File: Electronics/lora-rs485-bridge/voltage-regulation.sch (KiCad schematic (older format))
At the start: 5 parts, among them U4 MCP1810T-33I_OT

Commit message: Some PCB routing is done
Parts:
- C11: renamed from C?; footprint zive:C_0603_1608Metric -> Capacitor_SMD:C_0603_1608Metric
- C16, C7: footprint zive:C_0603_1608Metric -> Capacitor_SMD:C_0603_1608Metric
- R2: renamed from R?; footprint (none) -> Resistor_SMD:R_0603_1608Metric
- U4: footprint zive:SOT-23-5 -> Package_TO_SOT_SMD:SOT-23-5
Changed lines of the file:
@@
 EESchema Schematic File Version 5
-LIBS:lora-bridge-cache
 EELAYER 30 0
 EELAYER END
 $Descr A4 11693 8268
 encoding utf-8
-Sheet 4 5
+Sheet 3 5
 Title ""
 Date ""
@@
 F 0 "C7" H 3560 1771 50  0000 R CNN
 F 1 "4.7u" H 3560 1680 50  0000 R CNN
-F 2 "zive:C_0603_1608Metric" H 3713 1575 50  0001 C CNN
+F 2 "Capacitor_SMD:C_0603_1608Metric" H 3713 1575 50  0001 C CNN
 F 3 "~" H 3675 1725 50  0001 C CNN
 F 4 "CL10A475KP8NNNC" H 3675 1725 50  0001 C CNN "PartNo"
@@
 F 0 "U4" H 4600 2100 50  0000 C CNN
 F 1 "MCP1810T-33I_OT" H 4600 2009 50  0000 C CNN
-F 2 "zive:SOT-23-5" H 4625 1525 50  0001 C CNN
+F 2 "Package_TO_SOT_SMD:SOT-23-5" H 4625 1525 50  0001 C CNN
 F 3 "" H 4625 1525 50  0001 C CNN
 F 4 "MICROCHIP" H 4625 1725 50  0001 C CNN "Manufacturer"
@@
 F 0 "C16" H 3160 1771 50  0000 R CNN
 F 1 "4.7u" H 3160 1680 50  0000 R CNN
-F 2 "zive:C_0603_1608Metric" H 3313 1575 50  0001 C CNN
+F 2 "Capacitor_SMD:C_0603_1608Metric" H 3313 1575 50  0001 C CNN
 F 3 "~" H 3275 1725 50  0001 C CNN
 F 4 "CL10A475KP8NNNC" H 3275 1725 50  0001 C CNN "PartNo"
@@
 	5275 1575 5450 1575
 $Comp
-L Device:C C?
+L Device:C C11
 U 1 1 5D86D7BC
 P 5450 2025
-F 0 "C?" H 5335 2071 50  0000 R CNN
+F 0 "C11" H 5335 2071 50  0000 R CNN
 F 1 "4.7u" H 5335 1980 50  0000 R CNN
-F 2 "zive:C_0603_1608Metric" H 5488 1875 50  0001 C CNN
+F 2 "Capacitor_SMD:C_0603_1608Metric" H 5488 1875 50  0001 C CNN
 F 3 "~" H 5450 2025 50  0001 C CNN
 F 4 "CL10A475KP8NNNC" H 5450 2025 50  0001 C CNN "PartNo"
@@
 $EndComp
 $Comp
-L Device:R R?
+L Device:R R2
 U 1 1 5D86E8A3
 P 5450 1725
-F 0 "R?" H 5520 1771 50  0000 L CNN
+F 0 "R2" H 5520 1771 50  0000 L CNN
 F 1 "0" H 5520 1680 50  0000 L CNN
-F 2 "" V 5380 1725 50  0001 C CNN
+F 2 "Resistor_SMD:R_0603_1608Metric" V 5380 1725 50  0001 C CNN
 F 3 "~" H 5450 1725 50  0001 C CNN
 	1    5450 1725

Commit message: Add ESD protection to i2c lines, change VIN TVS diode to higher voltage, add series resistors to SPI lines, compress the PCB to be at width of typical 4xAA battery holder
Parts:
- removed R2: 0, Resistor_SMD:R_0603_1608Metric, symbol Device:R
- removed U4: MCP1810T-33I_OT, Package_TO_SOT_SMD:SOT-23-5, symbol miceuz:MCP1810T-33I_OT
- added U4: NCP718, TO_SOT_Packages_SMD:SOT-23-5, symbol miceuz:NCP718
- C11, C16, C7: Manufacturer SAMSUNG -> TDK; PartNo CL10A475KP8NNNC -> C1608X5R1C475K080AE
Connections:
- wire segments 9 -> 10
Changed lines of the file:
@@
 $Descr A4 11693 8268
 encoding utf-8
-Sheet 3 5
+Sheet 2 5
 Title ""
 Date ""
@@
 Text HLabel 4625 2175 3    50   Input ~ 0
 GND
-Text HLabel 5450 1575 2    50   Input ~ 0
-VOUT
 $Comp
 L Device:C C7
@@
 F 2 "Capacitor_SMD:C_0603_1608Metric" H 3713 1575 50  0001 C CNN
 F 3 "~" H 3675 1725 50  0001 C CNN
-F 4 "CL10A475KP8NNNC" H 3675 1725 50  0001 C CNN "PartNo"
-F 5 "SAMSUNG" H 3675 1725 50  0001 C CNN "Manufacturer"
+F 4 "C1608X5R1C475K080AE" H 3675 1725 50  0001 C CNN "PartNo"
+F 5 "TDK" H 3675 1725 50  0001 C CNN "Manufacturer"
 	1    3675 1725
 	1    0    0    -1
 $EndComp
-$Comp
-L miceuz:MCP1810T-33I_OT U4
-U 1 1 5C710FF3
-P 4625 1725
-F 0 "U4" H 4600 2100 50  0000 C CNN
-F 1 "MCP1810T-33I_OT" H 4600 2009 50  0000 C CNN
-F 2 "Package_TO_SOT_SMD:SOT-23-5" H 4625 1525 50  0001 C CNN
-F 3 "" H 4625 1525 50  0001 C CNN
-F 4 "MICROCHIP" H 4625 1725 50  0001 C CNN "Manufacturer"
-F 5 "MCP1810T-33I/OT" H 4625 1725 50  0001 C CNN "PartNo"
-	1    4625 1725
-	1    0    0    -1
-$EndComp
-Wire Wire Line
-	3925 1875 3925 1575
-Connection ~ 3925 1575
 Wire Wire Line
 	3675 1575 3925 1575
 Wire Wire Line
 	3675 1875 3675 2175
-Wire Wire Line
-	3675 2175 4625 2175
 $Comp
 L Device:C C16
@@
 F 2 "Capacitor_SMD:C_0603_1608Metric" H 3313 1575 50  0001 C CNN
 F 3 "~" H 3275 1725 50  0001 C CNN
-F 4 "CL10A475KP8NNNC" H 3275 1725 50  0001 C CNN "PartNo"
-F 5 "SAMSUNG" H 3275 1725 50  0001 C CNN "Manufacturer"
+F 4 "C1608X5R1C475K080AE" H 3275 1725 50  0001 C CNN "PartNo"
+F 5 "TDK" H 3275 1725 50  0001 C CNN "Manufacturer"
 	1    3275 1725
 	1    0    0    -1
@@
 	3275 1875 3275 2175
 Wire Wire Line
-	5450 2175 4625 2175
-Connection ~ 4625 2175
-Wire Wire Line
 	5275 1575 5450 1575
 $Comp
@@
 F 2 "Capacitor_SMD:C_0603_1608Metric" H 5488 1875 50  0001 C CNN
 F 3 "~" H 5450 2025 50  0001 C CNN
-F 4 "CL10A475KP8NNNC" H 5450 2025 50  0001 C CNN "PartNo"
-F 5 "SAMSUNG" H 5450 2025 50  0001 C CNN "Manufacturer"
+F 4 "C1608X5R1C475K080AE" H 5450 2025 50  0001 C CNN "PartNo"
+F 5 "TDK" H 5450 2025 50  0001 C CNN "Manufacturer"
 	1    5450 2025
 	1    0    0    -1
 $EndComp
+Wire Wire Line
+	3675 2175 4625 2175
 $Comp
-L Device:R R2
-U 1 1 5D86E8A3
-P 5450 1725
-F 0 "R2" H 5520 1771 50  0000 L CNN
-F 1 "0" H 5520 1680 50  0000 L CNN
-F 2 "Resistor_SMD:R_0603_1608Metric" V 5380 1725 50  0001 C CNN
-F 3 "~" H 5450 1725 50  0001 C CNN
-	1    5450 1725
+L miceuz:NCP718 U4
+U 1 1 5D8F1C6A
+P 4625 1725
+F 0 "U4" H 4600 2100 50  0000 C CNN
+F 1 "NCP718" H 4600 2009 50  0000 C CNN
+F 2 "TO_SOT_Packages_SMD:SOT-23-5" H 4625 1525 50  0001 C CNN
+F 3 "" H 4625 1525 50  0001 C CNN
+F 4 "NCP718ASN330T1G" H 4625 1725 50  0001 C CNN "PartNo"
+F 5 "ON SEMICONDUCTOR" H 4625 1725 50  0001 C CNN "Manufacturer"
+	1    4625 1725
 	1    0    0    -1
 $EndComp
+Wire Wire Line
+	3925 1875 3925 1575
+Connection ~ 3925 1575
+Text HLabel 5450 1575 2    50   Input ~ 0
+VOUT
+Wire Wire Line
+	5450 1875 5450 1575
+Connection ~ 4625 2175
+Wire Wire Line
+	4625 2175 5450 2175
 $EndSCHEMATC

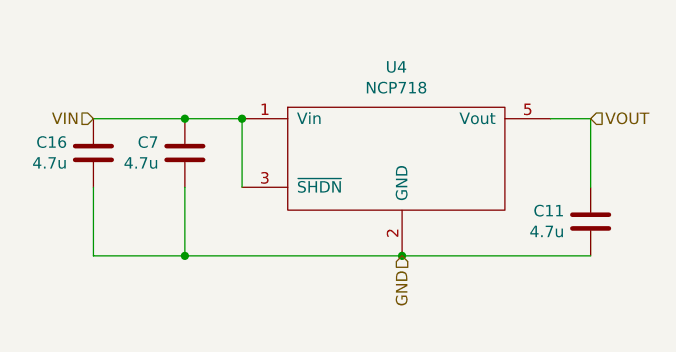
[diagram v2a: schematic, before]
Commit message: Add pullup to SWDCLK for better stability. Change reset pullup value to 1k
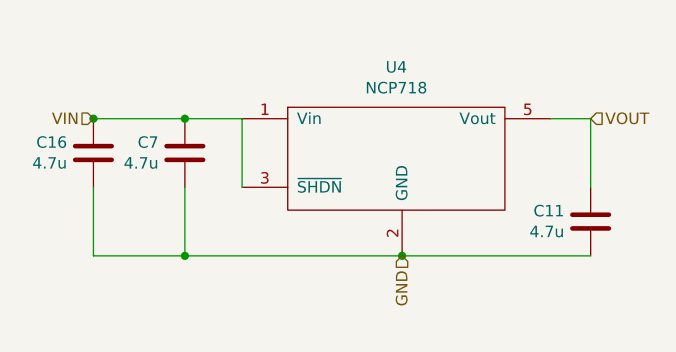
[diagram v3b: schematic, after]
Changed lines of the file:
@@
 $Descr A4 11693 8268
 encoding utf-8
-Sheet 2 5
+Sheet 5 5
 Title ""
 Date ""
@@
 Comment9 ""
 $EndDescr
+Wire Wire Line
+	3675 1875 3675 2175
+Wire Wire Line
+	3275 2175 3675 2175
+Connection ~ 3675 2175
+Wire Wire Line
+	3275 1875 3275 2175
 Text HLabel 3275 1575 0    50   Input ~ 0
 VIN
-Text HLabel 4625 2175 3    50   Input ~ 0
-GND
 $Comp
 L Device:C C7
@@
 Wire Wire Line
 	3675 1575 3925 1575
-Wire Wire Line
-	3675 1875 3675 2175
 $Comp
 L Device:C C16
@@
 $EndComp
 Wire Wire Line
-	3275 2175 3675 2175
-Connection ~ 3675 2175
-Wire Wire Line
 	3275 1575 3675 1575
 Connection ~ 3675 1575
 Wire Wire Line
-	3275 1875 3275 2175
+	3925 1875 3925 1575
+Connection ~ 3275 1575
 Wire Wire Line
 	5275 1575 5450 1575
@@
 	1    0    0    -1
 $EndComp
+Text HLabel 5450 1575 2    50   Input ~ 0
+VOUT
 Wire Wire Line
-	3675 2175 4625 2175
+	5450 1875 5450 1575
+Text HLabel 4625 2175 3    50   Input ~ 0
+GND
 $Comp
 L miceuz:NCP718 U4
@@
 $EndComp
 Wire Wire Line
-	3925 1875 3925 1575
-Connection ~ 3925 1575
-Text HLabel 5450 1575 2    50   Input ~ 0
-VOUT
-Wire Wire Line
-	5450 1875 5450 1575
+	3675 2175 4625 2175
 Connection ~ 4625 2175
 Wire Wire Line

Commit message: Update D3 to silicone diode as schottky leaks as hell; Add D2 to protect gates of mosfets; Remove series resistors from RFM95 interface, add pullups/downs for better sleep stability; Unify resistor values across the board; Bump version number to v1.2
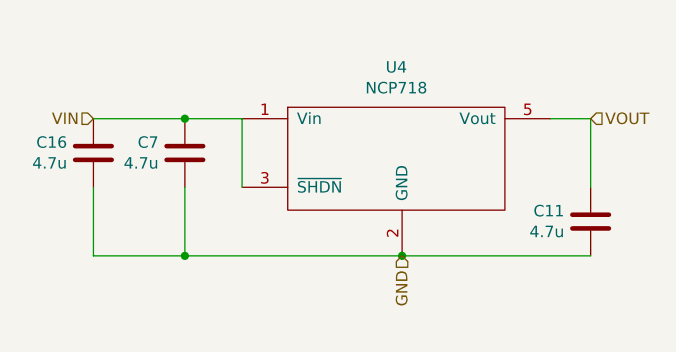
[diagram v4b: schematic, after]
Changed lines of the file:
@@
 $Descr A4 11693 8268
 encoding utf-8
-Sheet 5 5
+Sheet 3 5
 Title ""
 Date ""
@@
 Wire Wire Line
 	3925 1875 3925 1575
-Connection ~ 3275 1575
 Wire Wire Line
 	5275 1575 5450 1575

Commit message: Move R11 and accompanying components a bit so it's easier to replace it. Add fiducials. Generate gerbers for v1.2
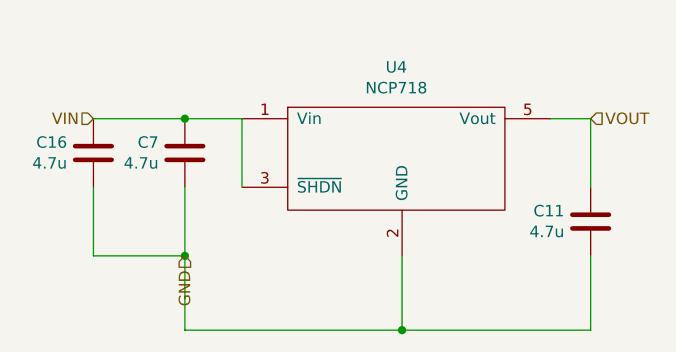
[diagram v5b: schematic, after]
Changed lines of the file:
@@
 $Descr A4 11693 8268
 encoding utf-8
-Sheet 3 5
+Sheet 2 5
 Title ""
 Date ""
@@
 Comment9 ""
 $EndDescr
-Wire Wire Line
-	3675 1875 3675 2175
-Wire Wire Line
-	3275 2175 3675 2175
-Connection ~ 3675 2175
-Wire Wire Line
-	3275 1875 3275 2175
 Text HLabel 3275 1575 0    50   Input ~ 0
 VIN
@@
 $EndComp
 Wire Wire Line
-	3675 1575 3925 1575
+	3275 1875 3275 2175
+Wire Wire Line
+	3275 2175 3675 2175
+Wire Wire Line
+	3675 1875 3675 2175
 $Comp
 L Device:C C16
@@
 	3925 1875 3925 1575
 Wire Wire Line
+	3675 1575 3925 1575
+Text HLabel 3675 2175 3    50   Input ~ 0
+GND
+Wire Wire Line
+	4625 2500 3675 2500
+Wire Wire Line
+	3675 2500 3675 2175
+Connection ~ 3675 2175
+Connection ~ 4625 2500
+Wire Wire Line
 	5275 1575 5450 1575
+Wire Wire Line
+	5450 1875 5450 1575
+Text HLabel 5450 1575 2    50   Input ~ 0
+VOUT
 $Comp
 L Device:C C11
@@
 	1    0    0    -1
 $EndComp
-Text HLabel 5450 1575 2    50   Input ~ 0
-VOUT
-Wire Wire Line
-	5450 1875 5450 1575
-Text HLabel 4625 2175 3    50   Input ~ 0
-GND
 $Comp
 L miceuz:NCP718 U4
@@
 $EndComp
 Wire Wire Line
-	3675 2175 4625 2175
-Connection ~ 4625 2175
+	4625 2175 4625 2500
 Wire Wire Line
-	4625 2175 5450 2175
+	4625 2500 5450 2500
+Wire Wire Line
+	5450 2500 5450 2175
 $EndSCHEMATC

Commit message: Move around vias so power planes are not so much broken. Move connectors closer together so all of them are on 5.08mm grid
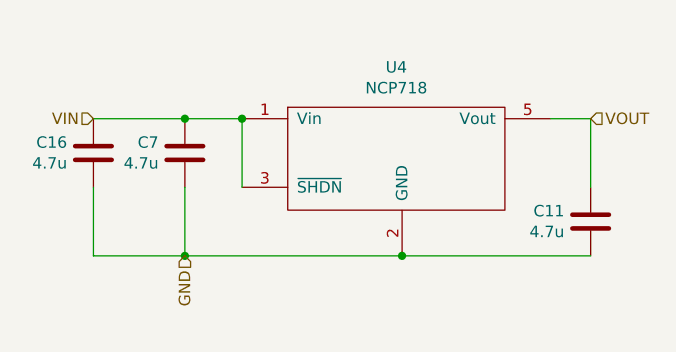
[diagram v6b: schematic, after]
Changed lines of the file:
@@
 $Descr A4 11693 8268
 encoding utf-8
-Sheet 2 5
+Sheet 4 5
 Title ""
 Date ""
@@
 Text HLabel 3275 1575 0    50   Input ~ 0
 VIN
+Wire Wire Line
+	3675 1575 3925 1575
+Wire Wire Line
+	3275 1575 3675 1575
+Connection ~ 3675 1575
 $Comp
 L Device:C C7
@@
 Wire Wire Line
 	3675 1875 3675 2175
+Text HLabel 3675 2175 3    50   Input ~ 0
+GND
+Wire Wire Line
+	3925 1875 3925 1575
 $Comp
 L Device:C C16
@@
 	1    0    0    -1
 $EndComp
-Wire Wire Line
-	3275 1575 3675 1575
-Connection ~ 3675 1575
-Wire Wire Line
-	3925 1875 3925 1575
-Wire Wire Line
-	3675 1575 3925 1575
-Text HLabel 3675 2175 3    50   Input ~ 0
-GND
-Wire Wire Line
-	4625 2500 3675 2500
-Wire Wire Line
-	3675 2500 3675 2175
 Connection ~ 3675 2175
-Connection ~ 4625 2500
-Wire Wire Line
-	5275 1575 5450 1575
-Wire Wire Line
-	5450 1875 5450 1575
 Text HLabel 5450 1575 2    50   Input ~ 0
 VOUT
@@
 	1    0    0    -1
 $EndComp
+Wire Wire Line
+	5275 1575 5450 1575
+Wire Wire Line
+	5450 1875 5450 1575
+Connection ~ 3925 1575
 $Comp
 L miceuz:NCP718 U4
@@
 $EndComp
 Wire Wire Line
-	4625 2175 4625 2500
+	3675 2175 4625 2175
+Connection ~ 4625 2175
 Wire Wire Line
-	4625 2500 5450 2500
-Wire Wire Line
-	5450 2500 5450 2175
+	4625 2175 5450 2175
 $EndSCHEMATC
